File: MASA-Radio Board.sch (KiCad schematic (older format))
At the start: 36 parts, among them IC1 FAN4010IL6X_F113, IC2 FAN4010IL6X_F113, J1 SC_19-20, J2 Conn_01x03_Male, J3 Conn_01x02, J4 Conn_01x06, J5 Conn_01x06, J6 Conn_01x02, J7 UJ2-MBH-1-SMT-TR, U1 MP5077GG-Z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

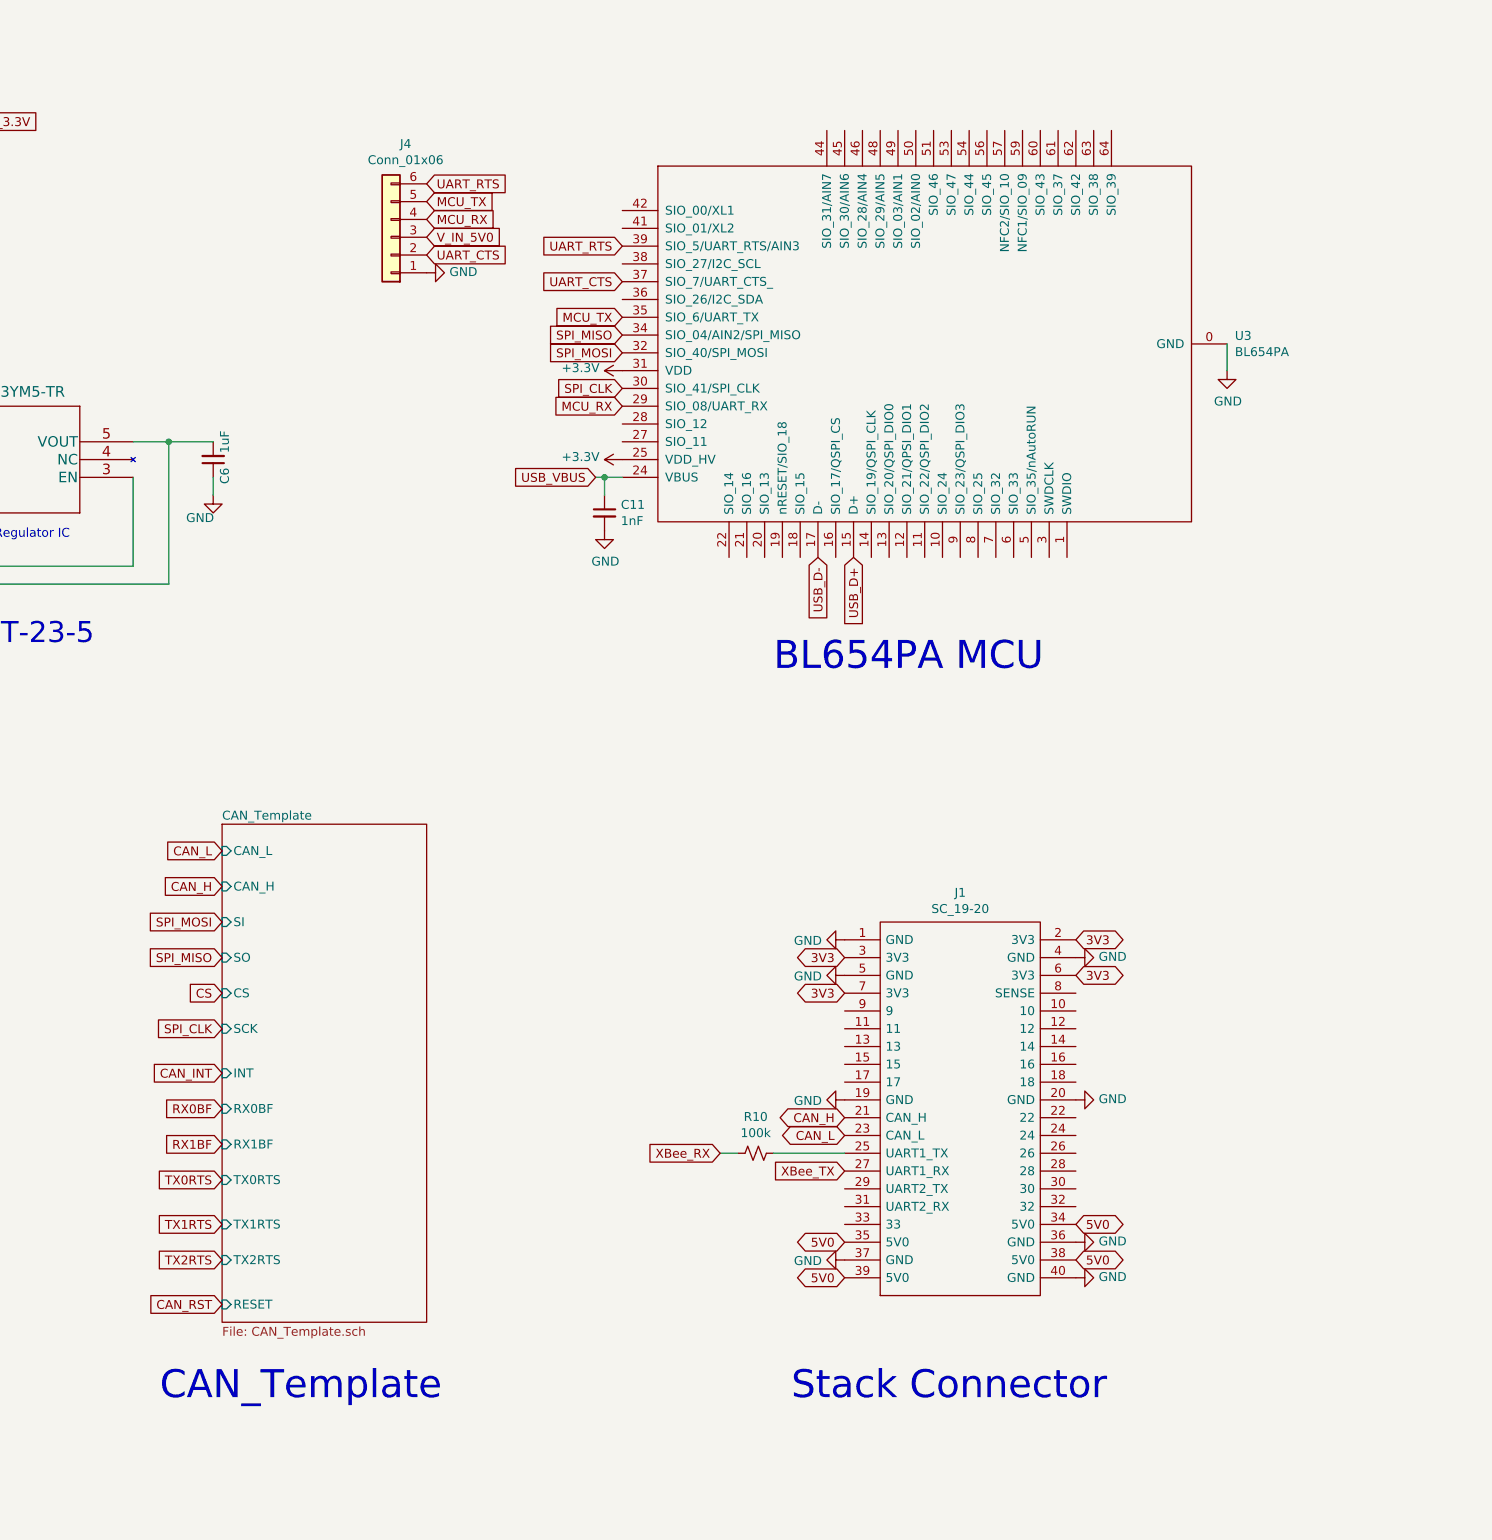
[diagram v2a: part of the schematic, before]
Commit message: Added nAutoRun header
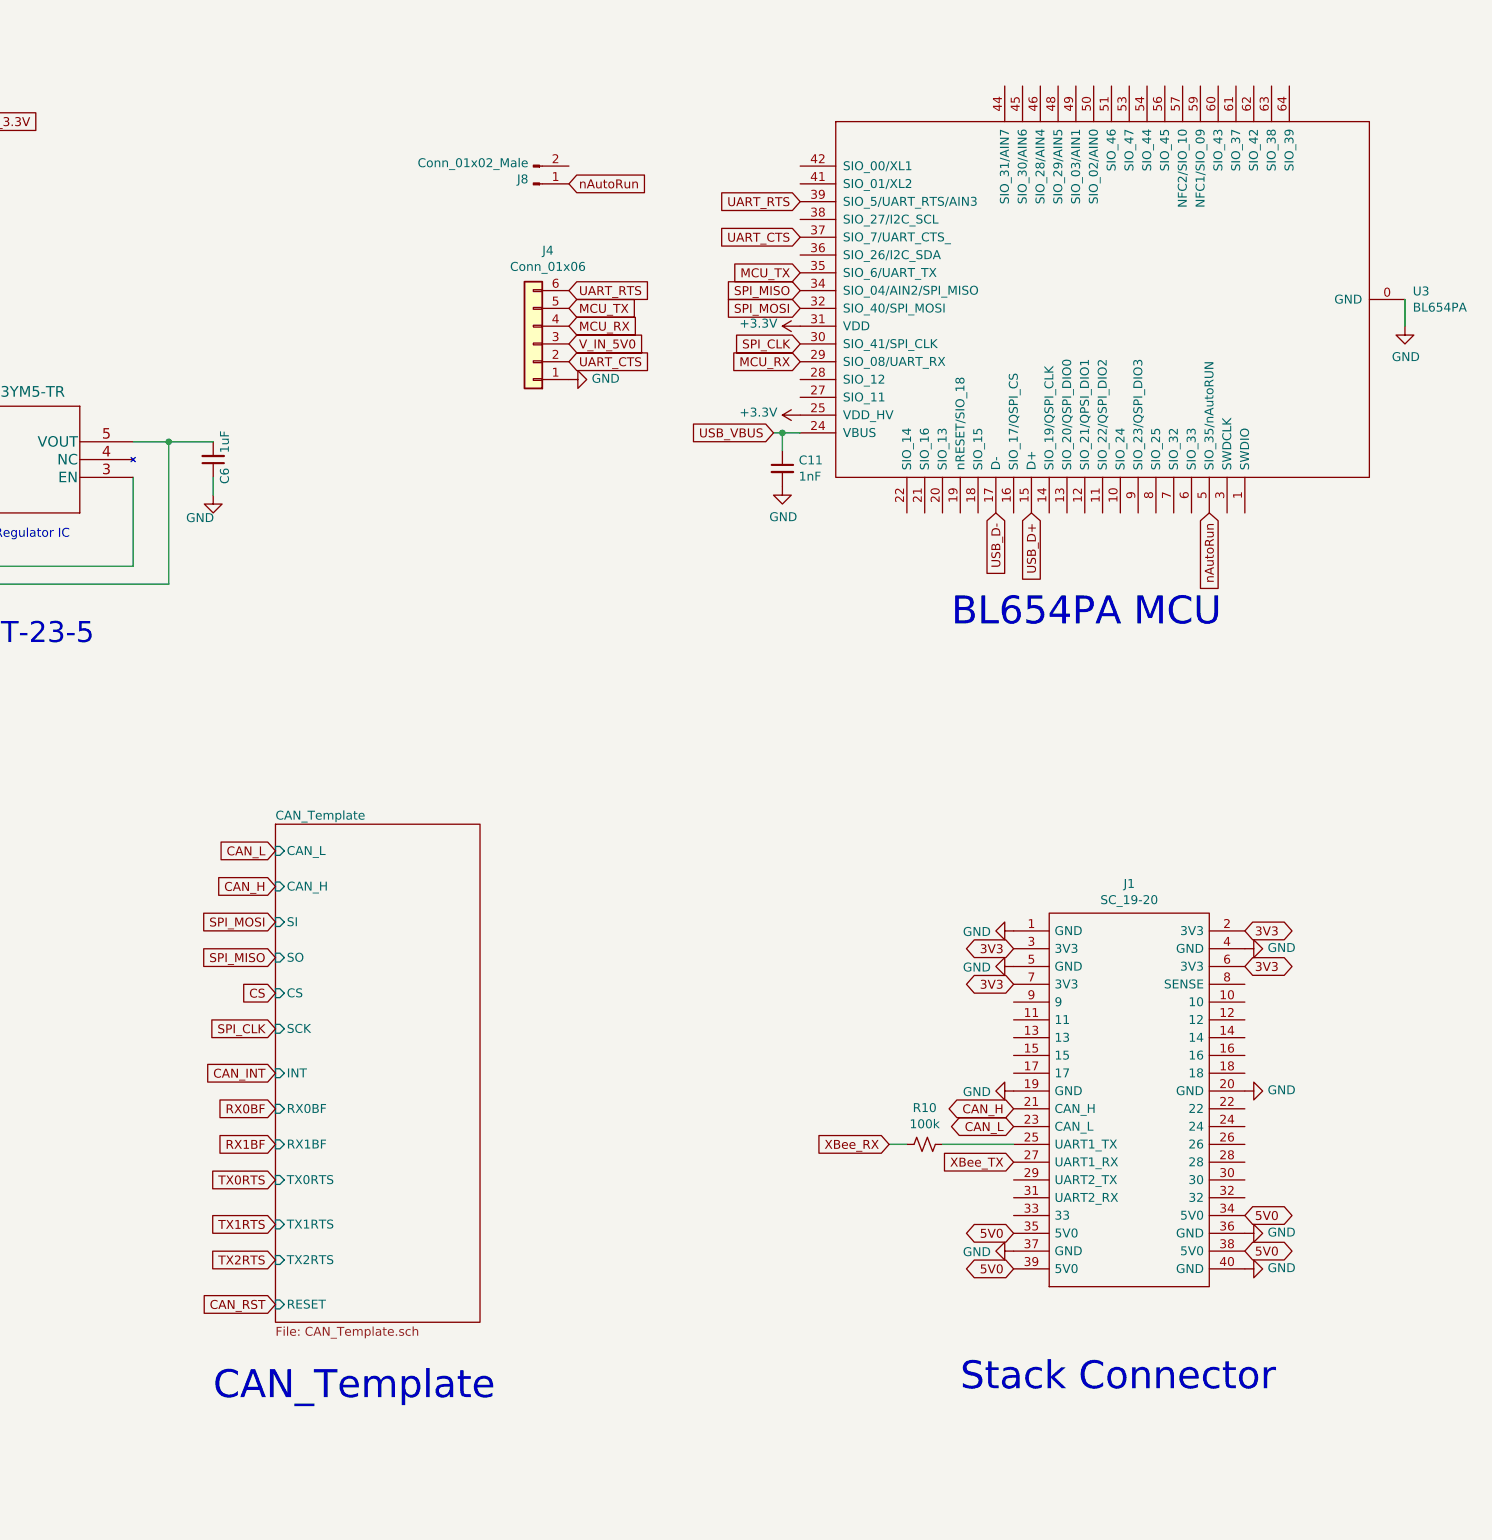
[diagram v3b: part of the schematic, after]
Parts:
- added J8: Conn_01x02_Male, symbol Connector:Conn_01x02_Male
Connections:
- net nAutoRun: now reaches U3.5 (SIO_35/nAutoRUN)
- net nAutoRun: now also J8.1 (Pin_1)
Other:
- moved on the sheet: C11, J1, J4, R10, U3

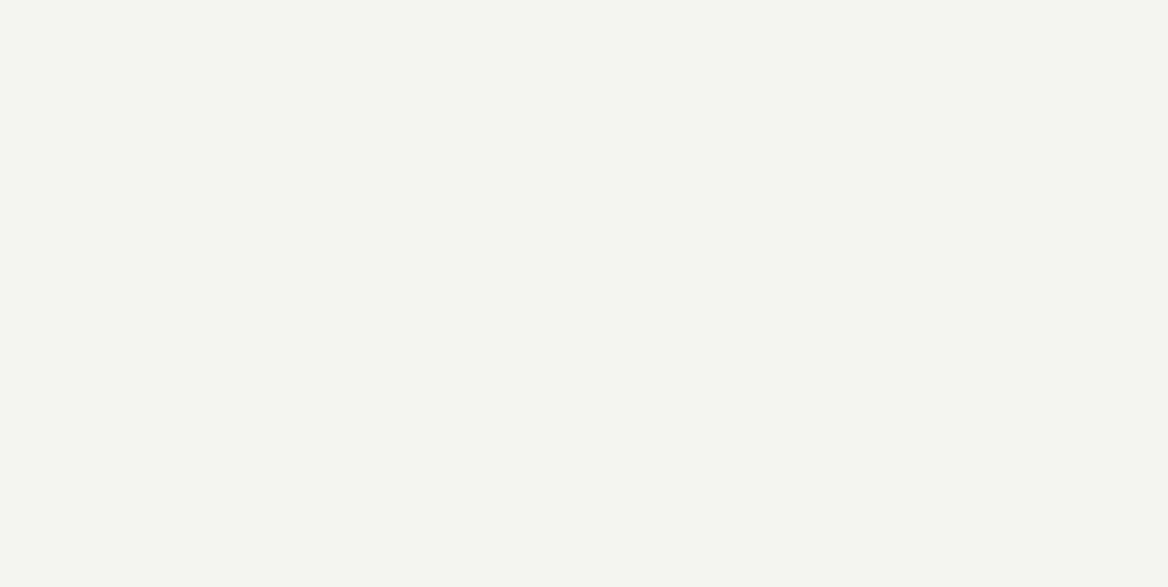
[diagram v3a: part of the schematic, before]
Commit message: Added Temp Sensor
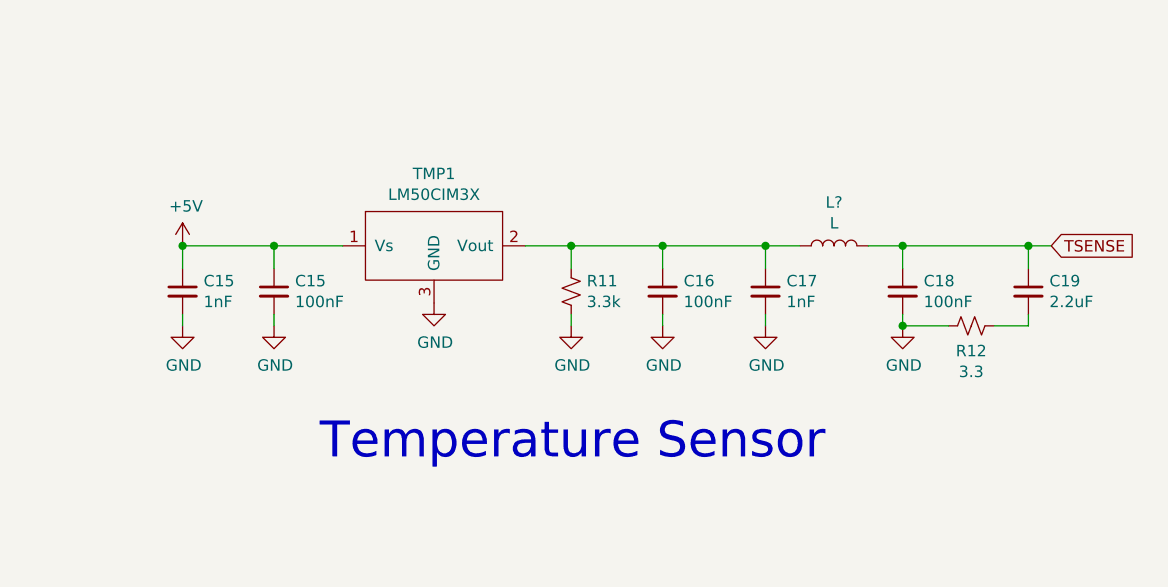
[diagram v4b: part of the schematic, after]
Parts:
- added C15, C16, C18: 100nF, symbol Device:C_Small
- added C15, C17: 1nF, symbol Device:C_Small
- added C19: 2.2uF, symbol Device:C_Small
- added L?: L, symbol Device:L
- added R11: 3.3k, symbol Device:R_Small_US
- added R12: 3.3, symbol Device:R_Small_US
- added TMP1: LM50CIM3X, Package_TO_SOT_SMD:SOT-23, symbol MASA_Library:LM50CIM3X
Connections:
- net +5V: now also C15.1, C15.1, TMP1.1 (Vs)
- net GND: now also C15.2, C15.2, C16.2, C17.2, C18.2, R11.2, R12.1, TMP1.3 (GND)
- new net: C16.1, C17.1, L?.1, R11.1, TMP1.2 (Vout)
- new net: C19.2, R12.2
- new net TSENSE: C18.1, C19.1, L?.2
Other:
- note added: "Temperature Sensor"

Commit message: Some minor adjustments
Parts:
- C11: value 1nF -> 4.7uF
- R1: value R -> 200k
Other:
- note added: "-CS\n-SCK\n-CAN_INT\n-RX0BF\n-RX1BF\n-TXORTS\n-TX1RTS\n-TX2RTS\n-CAN_RESET\n\n-TSENSE"
- note added: "Reserve I/O Pins for:"
- moved on the sheet: C10, C11, C12, C13, C14, C15, C16, C17, C18, C19, C6, C7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
